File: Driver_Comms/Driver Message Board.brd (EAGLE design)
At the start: 39.4 x 79.7 mm, 14 parts, among them U1 XBEE_PRO_S3B

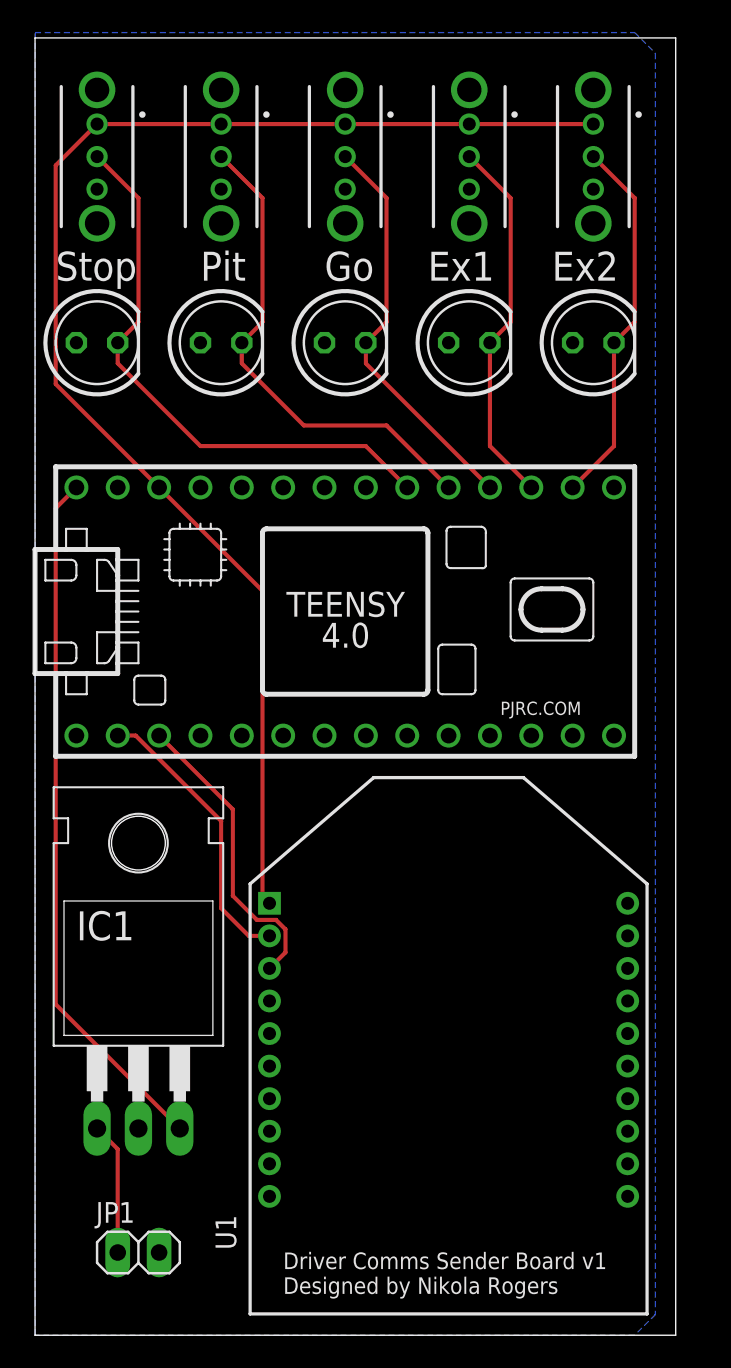
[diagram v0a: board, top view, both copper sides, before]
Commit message: Updated Sender Board
Corrected orientation of Xbee and also power supply.
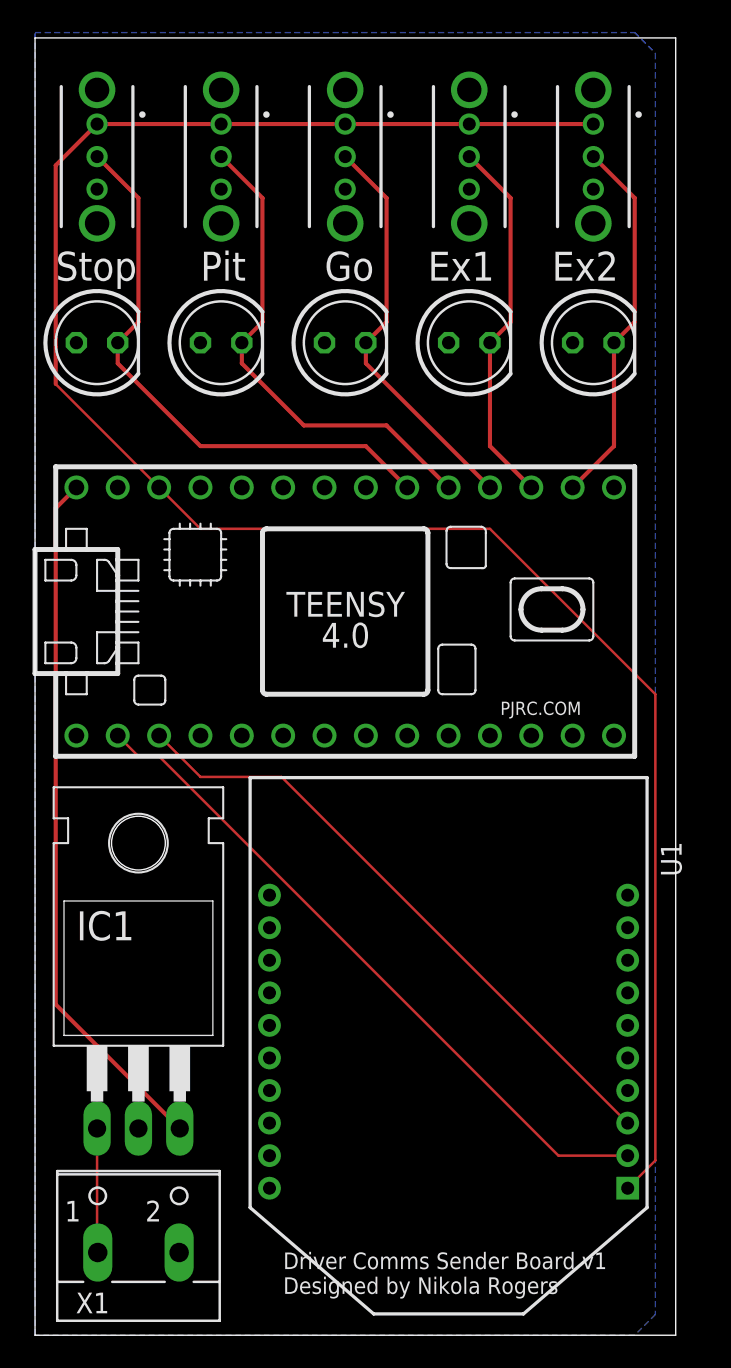
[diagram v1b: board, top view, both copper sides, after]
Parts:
- removed JP1: (no value), GTOR - Connectors:1X02
- added X1: (no value), con-wago-500:W237-102
- turned U1 to 180 degrees
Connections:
- net GND: now also X1.2; no longer JP1.2
- net VCC: now also X1.1; no longer JP1.1
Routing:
- net 3V_TEENSY: track 84.8 -> 123.3 mm
- net XBEE_TX: track 17.6 -> 42.0 mm
- net XBEE_RX: track 18.6 -> 38.6 mm
- net VCC: track 8.15 -> 7.64 mm
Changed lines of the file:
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@@
 <attribute name="VALUE" x="2.413" y="41.91" size="1.778" layer="27" ratio="10"/>
-</element>
-<element name="JP1" library="GTOR - Connectors" package="1X02" package3d_urn="urn:adsk.eagle:package:22435/2" value="" x="6.35" y="25.4" smashed="yes">
-<attribute name="NAME" x="3.7338" y="27.2288" size="1.27" layer="25" ratio="10"/>
-<attribute name="POPULARITY" value="98" x="72.39" y="-30.48" size="1.778" layer="27" display="off"/>
-<attribute name="VALUE" x="3.81" y="22.225" size="1.27" layer="27"/>
 </element>
 <element name="LED1" library="GTOR - Passive Components" package="LED-5MM" value="" x="34.29" y="81.28" smashed="yes">
@@
 </element>
 <element name="U$1" library="GTOR - Microcontroller" package="TEENSY_4.0_SIMPLE" value="TEENSY_4.0_SIMPLE" x="19.05" y="64.77" smashed="yes"/>
-<element name="U1" library="GTOR - Microcontroller" package="XBEE_PRO_S3B" value="XBEE_PRO_S3B" x="25.4" y="38.1" smashed="yes">
-<attribute name="DESCRIPTION" value=" General ISM &lt; 1GHz Transceiver Module 900MHz Antenna Not Included, RP-SMA Through Hole " x="53.34" y="20.32" size="1.778" layer="27" display="off"/>
-<attribute name="DIGI-KEY_PART_NUMBER" value="602-1293-ND" x="53.34" y="20.32" size="1.778" layer="27" display="off"/>
-<attribute name="MF" value="Digi International" x="53.34" y="20.32" size="1.778" layer="27" display="off"/>
-<attribute name="MP" value="XBP9B-XCST-001" x="53.34" y="20.32" size="1.778" layer="27" display="off"/>
-<attribute name="NAME" x="12.3589" y="25.5605" size="1.274009375" layer="25" rot="R90"/>
-<attribute name="PACKAGE" value="Module Digi International" x="53.34" y="20.32" size="1.778" layer="27" display="off"/>
-<attribute name="VALUE" x="34.588" y="28.8935" size="1.271609375" layer="27" rot="R90"/>
+<element name="U1" library="GTOR - Microcontroller" package="XBEE_PRO_S3B" value="XBEE_PRO_S3B" x="25.4" y="38.1" smashed="yes" rot="R180">
+<attribute name="DESCRIPTION" value=" General ISM &lt; 1GHz Transceiver Module 900MHz Antenna Not Included, RP-SMA Through Hole " x="-2.54" y="55.88" size="1.778" layer="27" rot="R180" display="off"/>
+<attribute name="DIGI-KEY_PART_NUMBER" value="602-1293-ND" x="-2.54" y="55.88" size="1.778" layer="27" rot="R180" display="off"/>
+<attribute name="MF" value="Digi International" x="-2.54" y="55.88" size="1.778" layer="27" rot="R180" display="off"/>
+<attribute name="MP" value="XBP9B-XCST-001" x="-2.54" y="55.88" size="1.778" layer="27" rot="R180" display="off"/>
+<attribute name="NAME" x="38.4411" y="50.6395" size="1.274009375" layer="25" rot="R270"/>
+<attribute name="PACKAGE" value="Module Digi International" x="-2.54" y="55.88" size="1.778" layer="27" rot="R180" display="off"/>
+<attribute name="VALUE" x="16.212" y="47.3065" size="1.271609375" layer="27" rot="R270"/>
+</element>
+<element name="X1" library="con-wago-500" library_urn="urn:adsk.eagle:library:195" package="W237-102" package3d_urn="urn:adsk.eagle:package:10688/1" value="" x="6.35" y="26.67" smashed="yes">
+<attribute name="MF" value="" x="6.35" y="26.67" size="1.778" layer="27" display="off"/>
+<attribute name="MPN" value="237-102" x="6.35" y="26.67" size="1.778" layer="27" display="off"/>
+<attribute name="NAME" x="2.5038" y="21.6662" size="1.27" layer="25" ratio="10"/>
+<attribute name="OC_FARNELL" value="unknown" x="6.35" y="26.67" size="1.778" layer="27" display="off"/>
+<attribute name="OC_NEWARK" value="70K9898" x="6.35" y="26.67" size="1.778" layer="27" display="off"/>
+<attribute name="POPULARITY" value="32" x="6.35" y="26.67" size="1.778" layer="27" display="off"/>
+<attribute name="VALUE" x="1.31" y="19.05" size="1.27" layer="27" ratio="10"/>
 </element>
 </elements>
 <signals>
 <signal name="VCC">
-<contactref element="JP1" pad="1"/>
 <contactref element="IC1" pad="1"/>
-<wire x1="3.81" y1="33.02" x2="5.08" y2="31.75" width="0.254" layer="1"/>
-<wire x1="5.08" y1="31.75" x2="5.08" y2="25.4" width="0.254" layer="1"/>
+<contactref element="X1" pad="1"/>
+<wire x1="3.85" y1="25.4" x2="3.81" y2="25.44" width="0.1524" layer="1"/>
+<wire x1="3.81" y1="25.44" x2="3.81" y2="33.02" width="0.1524" layer="1"/>
 </signal>
 <signal name="GND">
-<contactref element="JP1" pad="2"/>
 <contactref element="IC1" pad="2"/>
 <contactref element="U1" pad="10"/>
@@
 <vertex x="0" y="20.32"/>
 </polygon>
+<contactref element="X1" pad="2"/>
 </signal>
 <signal name="+5V">
@@
 <contactref element="U1" pad="2"/>
 <contactref element="U$1" pad="0/RX"/>
-<wire x1="11.43" y1="51.90315625" x2="6.18315625" y2="57.15" width="0.254" layer="1"/>
-<wire x1="6.18315625" y1="57.15" x2="5.08" y2="57.15" width="0.254" layer="1"/>
-<wire x1="13.13" y1="44.85" x2="14.4" y2="44.85" width="0.254" layer="1"/>
-<wire x1="13.13" y1="44.85" x2="11.43" y2="46.55" width="0.254" layer="1"/>
-<wire x1="11.43" y1="46.55" x2="11.43" y2="51.90315625" width="0.254" layer="1"/>
+<wire x1="36.4" y1="31.35" x2="32.15" y2="31.35" width="0.1524" layer="1"/>
+<wire x1="7.62" y1="55.88" x2="6.35" y2="55.88" width="0.1524" layer="1"/>
+<wire x1="6.35" y1="55.88" x2="5.08" y2="57.15" width="0.1524" layer="1"/>
+<wire x1="32.15" y1="31.35" x2="7.62" y2="55.88" width="0.1524" layer="1"/>
 </signal>
 <signal name="XBEE_RX">
 <contactref element="U1" pad="3"/>
 <contactref element="U$1" pad="1/TX"/>
-<wire x1="12.1506" y1="52.6194" x2="12.1506" y2="47.30426875" width="0.254" layer="1"/>
-<wire x1="7.62" y1="57.15" x2="12.1506" y2="52.6194" width="0.254" layer="1"/>
-<wire x1="15.3794" y1="45.25568125" x2="14.80568125" y2="45.8294" width="0.254" layer="1"/>
-<wire x1="13.62546875" y1="45.8294" x2="14.80568125" y2="45.8294" width="0.254" layer="1"/>
-<wire x1="12.1506" y1="47.30426875" x2="13.62546875" y2="45.8294" width="0.254" layer="1"/>
-<wire x1="14.4" y1="42.85" x2="15.3794" y2="43.8294" width="0.254" layer="1"/>
-<wire x1="15.3794" y1="43.8294" x2="15.3794" y2="45.25568125" width="0.254" layer="1"/>
+<wire x1="36.4" y1="33.35" x2="15.14" y2="54.61" width="0.1524" layer="1"/>
+<wire x1="10.16" y1="54.61" x2="7.62" y2="57.15" width="0.1524" layer="1"/>
+<wire x1="15.14" y1="54.61" x2="10.16" y2="54.61" width="0.1524" layer="1"/>
 </signal>
 <signal name="3V_TEENSY">
@@
 <contactref element="S4" pad="1"/>
 <contactref element="S5" pad="1"/>
-<wire x1="7.62" y1="72.39" x2="13.97" y2="66.04" width="0.254" layer="1"/>
-<wire x1="13.97" y1="47.28" x2="14.4" y2="46.85" width="0.254" layer="1"/>
-<wire x1="13.97" y1="66.04" x2="13.97" y2="47.28" width="0.254" layer="1"/>
 <wire x1="1.27" y1="92.17" x2="1.27" y2="78.74" width="0.254" layer="1"/>
-<wire x1="1.27" y1="78.74" x2="7.62" y2="72.39" width="0.254" layer="1"/>
 <wire x1="1.27" y1="92.17" x2="3.81" y2="94.71" width="0.254" layer="1"/>
 <wire x1="3.81" y1="94.71" x2="11.43" y2="94.71" width="0.254" layer="1"/>
@@
 <wire x1="19.05" y1="94.71" x2="26.67" y2="94.71" width="0.254" layer="1"/>
 <wire x1="26.67" y1="94.71" x2="34.29" y2="94.71" width="0.254" layer="1"/>
+<wire x1="36.4" y1="29.35" x2="38.1" y2="31.05" width="0.1524" layer="1"/>
+<wire x1="38.1" y1="31.05" x2="38.1" y2="59.69" width="0.1524" layer="1"/>
+<wire x1="38.1" y1="59.69" x2="27.94" y2="69.85" width="0.1524" layer="1"/>
+<wire x1="27.94" y1="69.85" x2="10.16" y2="69.85" width="0.1524" layer="1"/>
+<wire x1="10.16" y1="69.85" x2="7.62" y2="72.39" width="0.1524" layer="1"/>
+<wire x1="1.27" y1="78.74" x2="7.62" y2="72.39" width="0.1524" layer="1"/>
 </signal>
 <signal name="A0">
@@
 which will not be processed correctly with this version.
 </note>
+<note version="8.2" severity="warning">
+Since Version 8.2, EAGLE supports online libraries. The ids
+of those online libraries will not be understood (or retained)
+with this version.
+</note>
 <note version="8.3" severity="warning">

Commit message: Updated Driver Message Board so that LEDs work
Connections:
- net A0: now also LED1.A; no longer LED1.K
- net A1: now also LED2.A; no longer LED2.K
- net A2: now also LED3.A; no longer LED3.K
- net A3: now also LED4.A; no longer LED4.K
- net A4: now also LED5.A; no longer LED5.K
- net GND: now also LED1.K, LED2.K, LED3.K, LED4.K, LED5.K; no longer LED1.A, LED2.A, LED3.A, LED4.A, LED5.A
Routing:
- net A4: track 35.2 -> 38.1 mm
- net A3: track 30.1 -> 33.0 mm
- net A2: track 25.1 -> 27.9 mm
- net A1: track 23.0 -> 25.1 mm
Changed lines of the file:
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@@
 <contactref element="X1" pad="1"/>
 <wire x1="3.85" y1="25.4" x2="3.81" y2="25.44" width="0.1524" layer="1"/>
-<wire x1="3.81" y1="25.44" x2="3.81" y2="33.02" width="0.1524" layer="1"/>
+<wire x1="3.81" y1="25.44" x2="3.81" y2="33.02" width="0.254" layer="1"/>
 </signal>
 <signal name="GND">
@@
 <contactref element="U$1" pad="GND"/>
 <contactref element="S1" pad="3"/>
-<contactref element="LED1" pad="A"/>
 <contactref element="S2" pad="3"/>
-<contactref element="LED2" pad="A"/>
 <contactref element="S3" pad="3"/>
 <contactref element="S4" pad="3"/>
 <contactref element="S5" pad="3"/>
-<contactref element="LED3" pad="A"/>
-<contactref element="LED4" pad="A"/>
-<contactref element="LED5" pad="A"/>
 <polygon width="0.1524" layer="16">
 <vertex x="0" y="100.33"/>
@@
 </polygon>
 <contactref element="X1" pad="2"/>
+<contactref element="LED2" pad="K"/>
+<contactref element="LED1" pad="K"/>
+<contactref element="LED3" pad="K"/>
+<contactref element="LED4" pad="K"/>
+<contactref element="LED5" pad="K"/>
 </signal>
 <signal name="+5V">
@@
 <contactref element="U$1" pad="14/A0"/>
 <contactref element="S1" pad="2"/>
-<contactref element="LED1" pad="K"/>
 <wire x1="34.29" y1="92.71" x2="36.83" y2="90.17" width="0.254" layer="1"/>
-<wire x1="36.83" y1="90.17" x2="36.83" y2="82.55" width="0.254" layer="1"/>
-<wire x1="36.83" y1="82.55" x2="35.56" y2="81.28" width="0.254" layer="1"/>
-<wire x1="35.56" y1="81.28" x2="35.56" y2="74.93" width="0.254" layer="1"/>
-<wire x1="35.56" y1="74.93" x2="33.02" y2="72.39" width="0.254" layer="1"/>
+<contactref element="LED1" pad="A"/>
+<wire x1="36.83" y1="90.17" x2="36.83" y2="85.09" width="0.254" layer="1"/>
+<wire x1="36.83" y1="85.09" x2="33.02" y2="81.28" width="0.254" layer="1"/>
+<wire x1="33.02" y1="81.28" x2="33.02" y2="72.39" width="0.254" layer="1"/>
 </signal>
 <signal name="A1">
 <contactref element="U$1" pad="15/A1"/>
 <contactref element="S2" pad="2"/>
-<contactref element="LED2" pad="K"/>
 <wire x1="26.67" y1="92.71" x2="29.21" y2="90.17" width="0.254" layer="1"/>
-<wire x1="29.21" y1="90.17" x2="29.21" y2="82.55" width="0.254" layer="1"/>
-<wire x1="29.21" y1="82.55" x2="27.94" y2="81.28" width="0.254" layer="1"/>
-<wire x1="27.94" y1="81.28" x2="27.94" y2="74.93" width="0.254" layer="1"/>
-<wire x1="27.94" y1="74.93" x2="30.48" y2="72.39" width="0.254" layer="1"/>
+<contactref element="LED2" pad="A"/>
+<wire x1="29.21" y1="90.17" x2="29.21" y2="85.09" width="0.254" layer="1"/>
+<wire x1="29.21" y1="85.09" x2="25.4" y2="81.28" width="0.254" layer="1"/>
+<wire x1="25.4" y1="81.28" x2="30.48" y2="76.2" width="0.254" layer="1"/>
+<wire x1="30.48" y1="76.2" x2="30.48" y2="72.39" width="0.254" layer="1"/>
 </signal>
 <signal name="A2">
 <contactref element="U$1" pad="16/A2"/>
 <contactref element="S3" pad="2"/>
-<contactref element="LED3" pad="K"/>
 <wire x1="19.05" y1="92.71" x2="21.59" y2="90.17" width="0.254" layer="1"/>
-<wire x1="21.59" y1="90.17" x2="21.59" y2="82.55" width="0.254" layer="1"/>
-<wire x1="21.59" y1="82.55" x2="20.32" y2="81.28" width="0.254" layer="1"/>
-<wire x1="20.32" y1="81.28" x2="20.32" y2="80.01" width="0.254" layer="1"/>
-<wire x1="20.32" y1="80.01" x2="27.94" y2="72.39" width="0.254" layer="1"/>
+<contactref element="LED3" pad="A"/>
+<wire x1="21.59" y1="90.17" x2="21.59" y2="85.09" width="0.254" layer="1"/>
+<wire x1="21.59" y1="85.09" x2="17.78" y2="81.28" width="0.254" layer="1"/>
+<wire x1="25.4" y1="73.66" x2="26.67" y2="73.66" width="0.254" layer="1"/>
+<wire x1="26.67" y1="73.66" x2="27.94" y2="72.39" width="0.254" layer="1"/>
+<wire x1="17.78" y1="81.28" x2="25.4" y2="73.66" width="0.254" layer="1"/>
 </signal>
 <signal name="A3">
 <contactref element="U$1" pad="17/A3"/>
 <contactref element="S4" pad="2"/>
-<contactref element="LED4" pad="K"/>
 <wire x1="11.43" y1="92.71" x2="13.97" y2="90.17" width="0.254" layer="1"/>
-<wire x1="13.97" y1="90.17" x2="13.97" y2="82.55" width="0.254" layer="1"/>
-<wire x1="13.97" y1="82.55" x2="12.7" y2="81.28" width="0.254" layer="1"/>
-<wire x1="12.7" y1="81.28" x2="12.7" y2="80.01" width="0.254" layer="1"/>
-<wire x1="12.7" y1="80.01" x2="16.51" y2="76.2" width="0.254" layer="1"/>
 <wire x1="21.59" y1="76.2" x2="25.4" y2="72.39" width="0.254" layer="1"/>
-<wire x1="16.51" y1="76.2" x2="21.59" y2="76.2" width="0.254" layer="1"/>
+<contactref element="LED4" pad="A"/>
+<wire x1="13.97" y1="90.17" x2="13.97" y2="85.09" width="0.254" layer="1"/>
+<wire x1="13.97" y1="85.09" x2="10.16" y2="81.28" width="0.254" layer="1"/>
+<wire x1="10.16" y1="81.28" x2="15.24" y2="76.2" width="0.254" layer="1"/>
+<wire x1="15.24" y1="76.2" x2="21.59" y2="76.2" width="0.254" layer="1"/>
 </signal>
 <signal name="A4">
 <contactref element="U$1" pad="18/A4/SDA"/>
 <contactref element="S5" pad="2"/>
-<contactref element="LED5" pad="K"/>
-<wire x1="6.35" y1="90.17" x2="6.35" y2="82.55" width="0.254" layer="1"/>
-<wire x1="6.35" y1="82.55" x2="5.08" y2="81.28" width="0.254" layer="1"/>
 <wire x1="3.81" y1="92.71" x2="6.35" y2="90.17" width="0.254" layer="1"/>
-<wire x1="5.08" y1="81.28" x2="5.08" y2="80.01" width="0.254" layer="1"/>
-<wire x1="5.08" y1="80.01" x2="10.16" y2="74.93" width="0.254" layer="1"/>
-<wire x1="10.16" y1="74.93" x2="20.32" y2="74.93" width="0.254" layer="1"/>
 <wire x1="20.32" y1="74.93" x2="22.86" y2="72.39" width="0.254" layer="1"/>
+<contactref element="LED5" pad="A"/>
+<wire x1="6.35" y1="90.17" x2="6.35" y2="85.09" width="0.254" layer="1"/>
+<wire x1="6.35" y1="85.09" x2="2.54" y2="81.28" width="0.254" layer="1"/>
+<wire x1="2.54" y1="81.28" x2="8.89" y2="74.93" width="0.254" layer="1"/>
+<wire x1="8.89" y1="74.93" x2="20.32" y2="74.93" width="0.254" layer="1"/>
 </signal>
 </signals>
